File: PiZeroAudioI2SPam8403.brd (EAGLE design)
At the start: 65.1 x 30.2 mm, 46 parts, among them CON1 RPI-ZERO, J1 GROVE, J2 2X2HEADER, J3 2X1-LOCKING, J4 GROVE, J5 4X1-LOCKING, Q1 DMG2305UX, U1 TXB0104PWR, U2 LSM6DS33, U3 PCM5101A, U4 DMMT5401, U5 TXS0102, U6 PAM8403

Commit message: Fit Charger Parts
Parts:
- added C21: 4.7uF, SparkFun-Capacitors:0603
- added C25: 22uF, SparkFun-Capacitors:0805
- added D4: BLUE, SparkFun-LED:LED-0603
- added FRAME1: FRAME-LETTER, SparkFun-Aesthetics:CREATIVE_COMMONS
- added J10: (no value), SparkFun-Connectors:1X01
- added J11: AMP FCI 10103594-0001LF, SparkFun-Connectors:USB-MICROB-PTH
- added J8: JST, SparkFun-Connectors:JST-2-SMD
- added L1: 2.2UH3A, SparkFun-Coils:INDUCTOR_4X4MM
- added R10: 1k, SparkFun-Resistors:0603
- added R11, R15: 750K, SparkFun-Resistors:0603
- added R12: 100k, SparkFun-Resistors:0603
- added R13: DNP, SparkFun-Resistors:0603
- added RPROG: 2.0k, SparkFun-Resistors:0603
- added TP1: TEST-POINT3, SparkFun-Connectors:PAD.03X.03
- added U7: MCP73831, SparkFun-IC-Power:SOT23-5
- added U8: PAM2401, SparkFun-IC-Power:MSOP8
- moved U4 27.7 mm to (-70.6, 3.96)
- moved Q1 27.7 mm to (-66.7, 6.91)
- moved R7 27.7 mm to (-69.9, 6.58)
- moved R8 27.7 mm to (-66.8, 3.15)
- moved C17 25.1 mm to (-47.8, 19.8), turned to 0 degrees
- moved C16 23.9 mm to (-56.1, 19.5), turned to 180 degrees
- moved C18 23.7 mm to (-42.4, 11.4), turned to 90 degrees
- moved C20 23.7 mm to (-52.1, 19.6)
- moved C19 22.3 mm to (-59.3, 15.8), turned to 0 degrees
- moved J5 15.0 mm to (-36.7, 4.72)
- moved J3 10.6 mm to (-45.0, 4.72)
- moved U6 0.70 mm to (-48.9, 13.6)
- moved R9 0.18 mm to (-51.1, 22.9)
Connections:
- new net +5VCHARGE: C21.1, J11.VBUS, Q1.D, R10.2, U4.E2, U7.4
- new net EN: J10.1, R15.1, U8.2
- new net N$15: RPROG.1, U7.5
- new net N$16: D4.C, TP1.P$1, U7.1
- new net N$17: R11.1, R12.2, U8.5
- new net N$18: L1.P$2, U8.1
- new net N$19: R13.2, U8.6
- new net N$23: D4.A, R10.1
- new net VBATT: C25.1, J8.2, L1.P$1, R15.2, U7.3, U8.3
- net +5V: now also R11.2, U8.7; no longer Q1.D, U4.E2
- net AGND: now also C21.2, C25.2, J11.GND, J8.1, R12.1, R13.1, RPROG.2, U7.2, U8.4, U8.8
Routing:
- net +5V: track 58.3 -> 40.5 mm
- net AGND: track 66.7 -> 57.2 mm
- net GND: track 201.3 -> 196.3 mm
- net SCL-OUT: track 84.2 -> 80.5 mm
- net +5V-IN: track 7.00 -> 4.38 mm
- net SDA-OUT: track 55.0 -> 53.9 mm

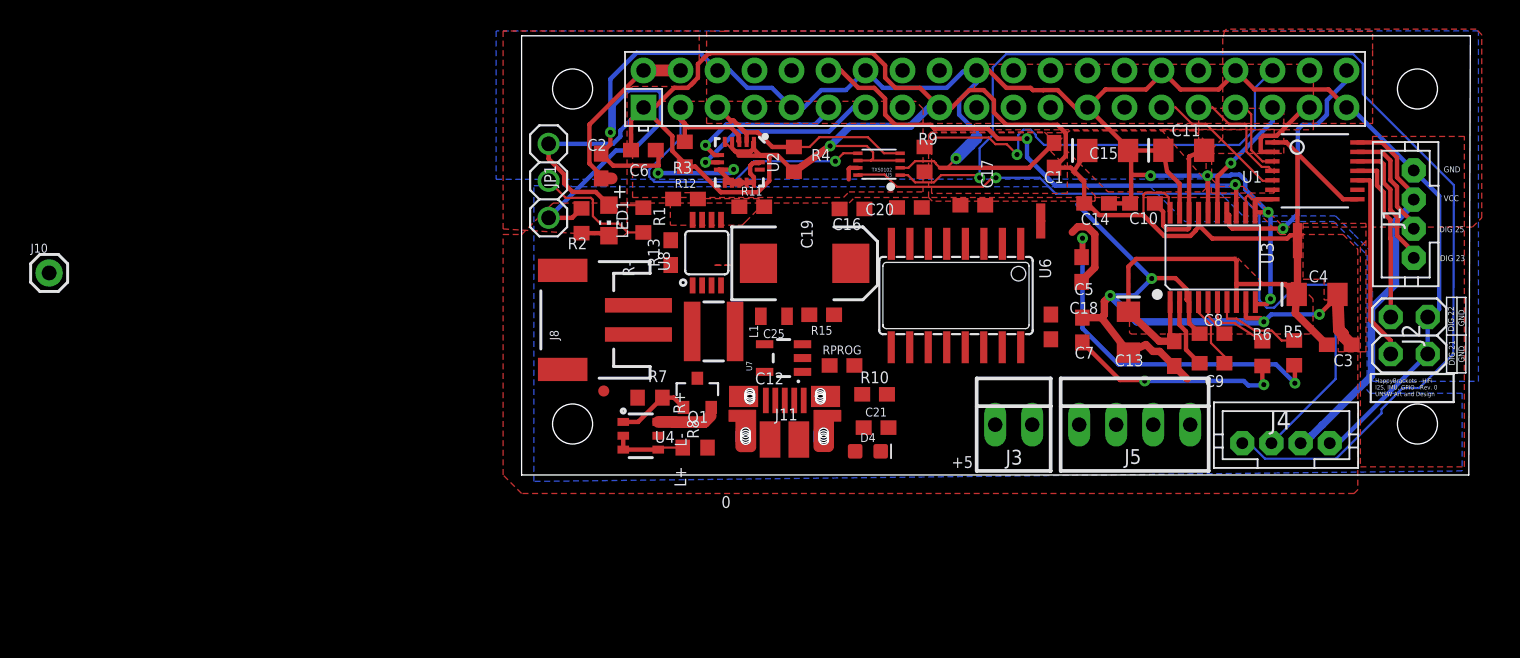
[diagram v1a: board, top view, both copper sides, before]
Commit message: Routed to Audio
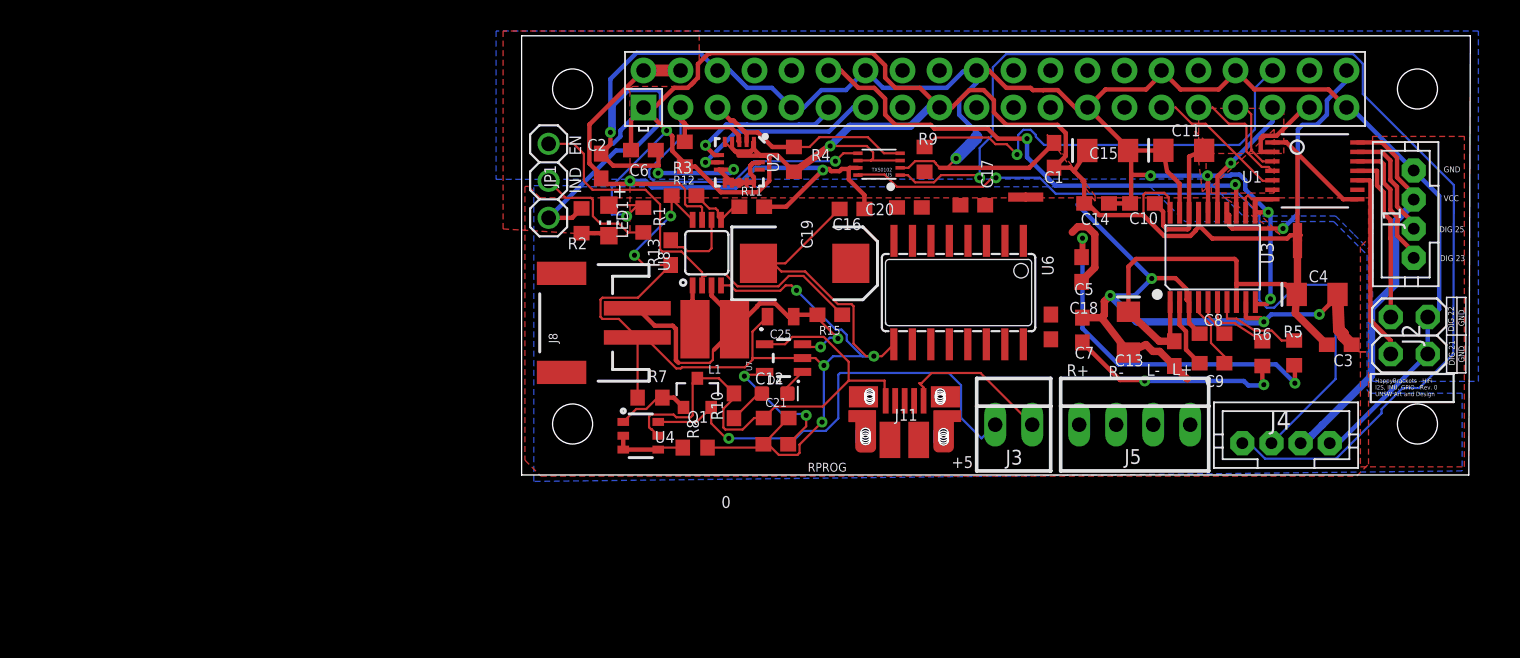
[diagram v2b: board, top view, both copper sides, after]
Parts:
- removed J10: (no value), SparkFun-Connectors:1X01
- removed TP1: TEST-POINT3, SparkFun-Connectors:PAD.03X.03
- L1: value 2.2UH3A -> IFSC1515AHER2R2M01; device SparkFun-Coils:INDUCTOR_4X4MM -> HappyBrackets:IND_IFSC_1515AH
- moved R10 9.68 mm to (-64.2, 6.02), turned to 90 degrees
- moved J11 8.23 mm to (-52.5, 5.03)
- moved D4 7.53 mm to (-61.4, 6.86)
- moved RPROG 7.07 mm to (-61.3, 3.38), turned to 180 degrees
- moved C21 6.89 mm to (-61.3, 5.18)
- moved SH2 1.85 mm to (-44.1, 20.3), turned to 0 degrees
- moved R15 0.56 mm to (-57.6, 12.3)
- moved C25 0.46 mm to (-61.0, 12.1)
- moved U6 0.27 mm to (-48.7, 13.8)
- moved R12 0.25 mm to (-67.6, 20.4)
- moved J8 0.22 mm to (-74.5, 11.7)
- moved L1 0.17 mm to (-65.5, 11.3), turned to 180 degrees
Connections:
- net N$10 renamed L-
- net N$13 renamed R-
- net N$14 renamed R+
- net N$8 renamed L+
- net +3V3: no longer JP1.1
- net AGND: now also C18.2, C19.-
- net EN: now also JP1.1; no longer J10.1
- net GND: no longer C18.2, C19.-
- net N$16: no longer TP1.P$1
- net N$18: now also L1.2; no longer L1.P$2
- net VBATT: now also L1.1; no longer L1.P$1
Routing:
- net AGND: track 57.2 -> 164.5 mm, vias 4 -> 10
- net +5VCHARGE: track 0.04 -> 35.1 mm
- net +5V: track 40.5 -> 73.7 mm, vias 0 -> 2
- net EN: track 0.00 -> 29.4 mm
- net +5V-IN: track 4.38 -> 32.2 mm, vias 0 -> 1
- net VBATT: track 0.00 -> 26.3 mm, vias 0 -> 2
- net N$15: track 0.00 -> 9.43 mm, vias 0 -> 2
- net N$19: track 0.00 -> 5.15 mm
- net N$17: track 0.00 -> 4.37 mm
- net N$18: track 0.00 -> 3.08 mm
- net N$23: track 0.00 -> 2.62 mm
- net N$16: track 0.00 -> 1.92 mm
- net +3V3: track 141.0 -> 139.3 mm, vias 1 -> 3
- removed copper zone on layer 1, net +3V3
- removed copper zone on layer 1, net +5V
- removed copper zone on layer 1, net AN3V3
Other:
- board text added: "EN"
- board text added: "IND"

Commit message: Routed with ratsnest
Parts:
- moved C18 1.78 mm to (-42.6, 9.67), turned to 270 degrees
- moved C5 1.24 mm to (-39.1, 15.7)
- moved C7 1.17 mm to (-39.1, 11.1)
- moved SH2 0.94 mm to (-44.1, 21.3), turned to 180 degrees
- moved C20 0.78 mm to (-52.9, 19.5), turned to 180 degrees
- moved C17 0.44 mm to (-47.5, 19.4)
- moved U6 0.33 mm to (-49.0, 13.6)
- moved C13 0.18 mm to (-36.9, 11.1)
- turned C16 to 0 degrees
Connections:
- net R+: now also J5.2; no longer J5.1
- net R-: now also J5.1; no longer J5.2
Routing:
- net AGND: track 164.5 -> 230.4 mm, vias 10 -> 20
- net +5V: track 73.7 -> 128.6 mm, vias 2 -> 3
- net AN3V3: track 32.2 -> 78.9 mm, vias 0 -> 3
- net AUDIO-RIGHT: track 25.1 -> 52.9 mm
- net AUDIO-LEFT: track 15.0 -> 35.6 mm, vias 2 -> 3
- net GND: track 196.3 -> 216.7 mm, vias 8 -> 10
- net L-: track 0.00 -> 20.1 mm
- net L+: track 0.00 -> 19.9 mm
- net N$5: track 0.00 -> 13.8 mm, vias 0 -> 2
- net R+: track 0.00 -> 10.4 mm
- net R-: track 0.00 -> 10.3 mm
- net +3V3: track 139.3 -> 135.3 mm
- net N$7: track 0.00 -> 2.97 mm
- added copper zone on layer 1, net +3V
- added copper zone on layer 1, net +5V

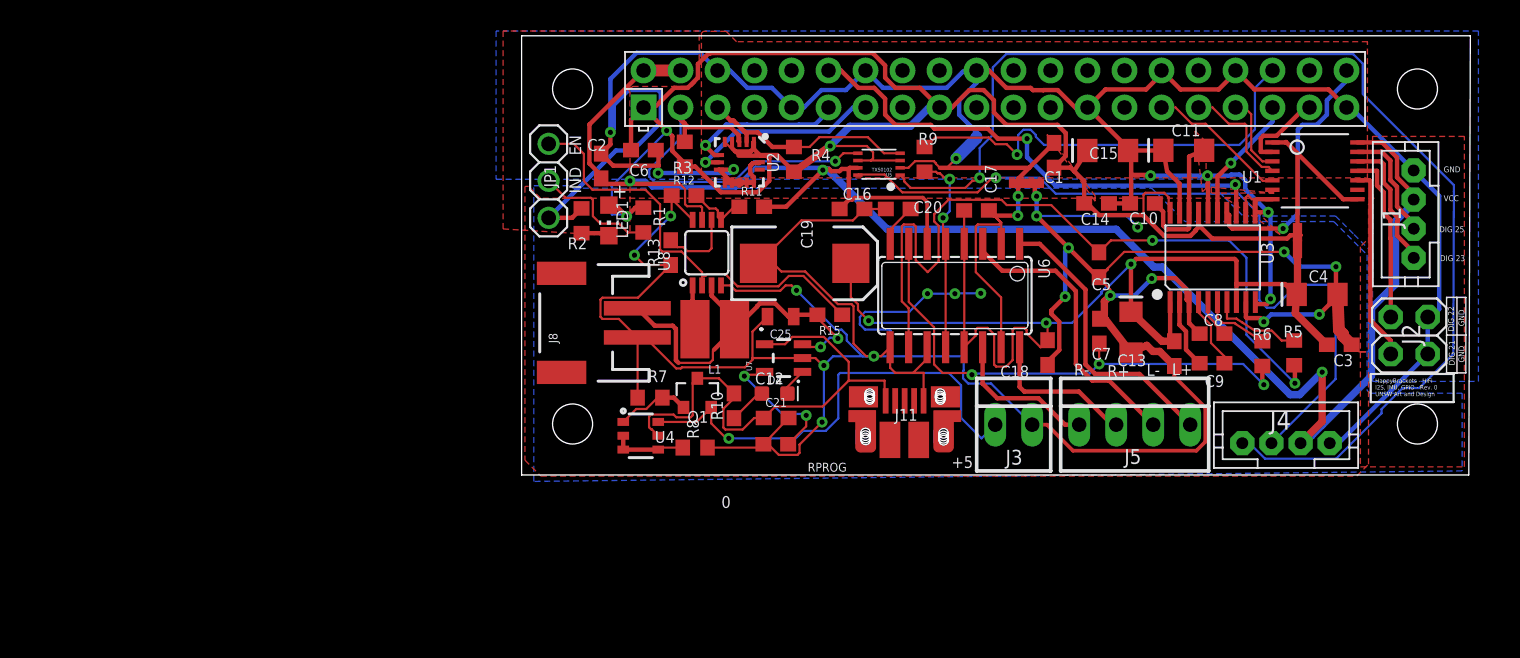
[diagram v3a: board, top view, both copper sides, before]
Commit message: Changed Footprints for consistency
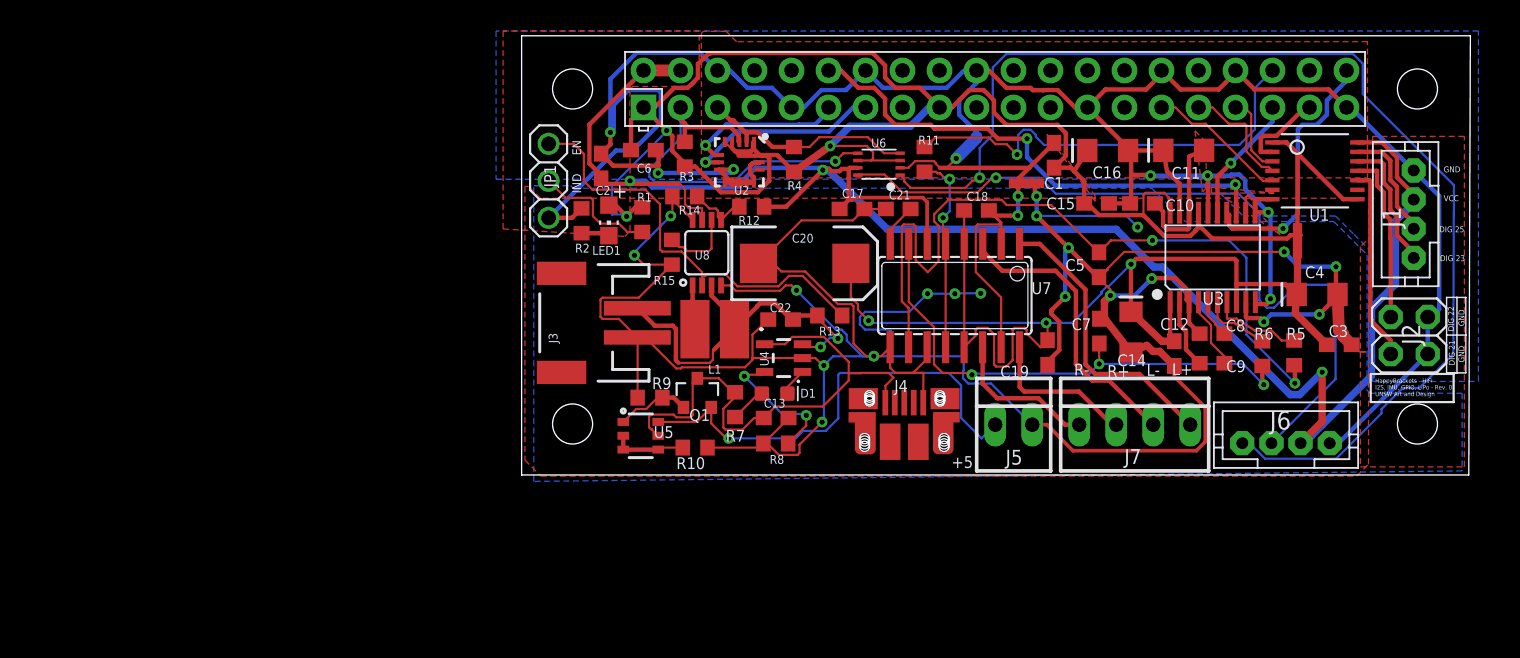
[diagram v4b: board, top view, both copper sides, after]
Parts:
- removed C25: 22uF, SparkFun-Capacitors:0805
- removed FRAME1: FRAME-LETTER, SparkFun-Aesthetics:CREATIVE_COMMONS
- removed J11: AMP FCI 10103594-0001LF, SparkFun-Connectors:USB-MICROB-PTH
- removed J8: JST, SparkFun-Connectors:JST-2-SMD
- removed RPROG: 2.0k, SparkFun-Resistors:0603
- added C22: 22uF, resistor:C0603
- added J6: GROVE, HappyBrackets:JST-PH4
- added J7: 4X1-LOCKING, HappyBrackets:22-23-2041
- added R14: 100k, adafruit:R0603
- C13: value 10uF -> 4.7uF; device HappyBrackets:EIA3216 -> SparkFun-Capacitors:0603
- C14: value 0.1uF -> 10uF; device rcl:C0603 -> HappyBrackets:EIA3216
- C15: value 10uF -> 0.1uF; device HappyBrackets:EIA3216 -> rcl:C0603
- C16: value 1uF -> 10uF; device rcl:C0603 -> HappyBrackets:EIA3216
- C19: value 470uF -> 1uF; device HappyBrackets:EIA7343 -> rcl:C0603
- C20: value 0.1uF -> 470uF; device rcl:C0603 -> HappyBrackets:EIA7343
- C21: value 4.7uF -> 0.1uF; device SparkFun-Capacitors:0603 -> rcl:C0603
- J3: value 2X1-LOCKING -> JST; device HappyBrackets:22-23-2021 -> SparkFun-Connectors:JST-2-SMD
- J4: value GROVE -> AMP FCI 10103594-0001LF; device HappyBrackets:JST-PH4 -> HappyBrackets:USB-MICROB-PTH
- J5: value 4X1-LOCKING -> 2X1-LOCKING; device HappyBrackets:22-23-2041 -> HappyBrackets:22-23-2021
- R10: value 1k -> 10K; device SparkFun-Resistors:0603 -> adafruit:R0603
- R11: value 750K -> 10K; device SparkFun-Resistors:0603 -> adafruit:R0603
- R12: value 100k -> 750K; device SparkFun-Resistors:0603 -> adafruit:R0603
- R13: value DNP -> 750K; device SparkFun-Resistors:0603 -> adafruit:R0603
- R15: value 750K -> DNP; device SparkFun-Resistors:0603 -> adafruit:R0603
- R7: value 47K -> 1k
- R8: value 10K -> 2.0k
- R9: value 10K -> 47K
- U4: value DMMT5401 -> MCP73831; device HappyBrackets:SOT26-TRANS -> SparkFun-IC-Power:SOT23-5
- U5: value TXS0102 -> DMMT5401; device adafruit:VFSOP-8 -> HappyBrackets:SOT26-TRANS
- U6: value PAM8403 -> TXS0102; device HappyBrackets:SOP-16 -> adafruit:VFSOP-8
- U7: value MCP73831 -> PAM8403; device SparkFun-IC-Power:SOT23-5 -> HappyBrackets:SOP-16
- moved J3 30.4 mm to (-74.5, 11.7), turned to 90 degrees
- moved J4 26.4 mm to (-52.5, 6.25)
- moved C13 25.1 mm to (-61.3, 5.18), turned to 0 degrees
- moved R9 25.0 mm to (-69.9, 6.58), turned to 180 degrees
- moved U5 24.8 mm to (-70.6, 3.96), turned to 270 degrees
- moved C16 18.0 mm to (-38.5, 23.5), turned to 180 degrees
- moved C19 17.8 mm to (-42.6, 9.67), turned to 270 degrees
- moved C21 16.6 mm to (-52.9, 19.5), turned to 180 degrees
- moved U7 12.5 mm to (-49.0, 13.6), turned to 180 degrees
- moved R11 12.3 mm to (-51.1, 22.9), turned to 270 degrees
- moved R13 11.7 mm to (-57.6, 12.2), turned to 180 degrees
- moved R15 11.7 mm to (-68.4, 16.6), turned to 90 degrees
- moved U4 11.2 mm to (-60.8, 9.30), turned to 90 degrees
- moved C18 10.9 mm to (-47.5, 19.4), turned to 0 degrees
- moved U6 10.4 mm to (-54.2, 22.6), turned to 90 degrees
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- renumbered D4 to D1
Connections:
- net +3V3: now also C15.2, C16.+, U6.P$3, U6.P$6; no longer C14.2, C15.+, U5.P$3, U5.P$6
- net +5V: now also C17.1, J6.3, R12.2, U6.P$7, U7.6; no longer C16.1, J4.3, R11.2, U5.P$7, U6.6
- net +5V-IN: now also J5.1, U5.E1; no longer J3.1, U4.E1
- net +5VCHARGE: now also C13.1, J4.VBUS, R7.2, U4.4, U5.E2; no longer C21.1, J11.VBUS, R10.2, U4.E2, U7.4
- net /MUTE: now also R11.1; no longer R9.1
- net AGND: now also C13.2, C14.-, C17.2, C19.2, C20.-, C22.2, J3.1, J4.GND, J5.2, R10.2, R14.1, R15.1, R9.2, U4.2, U7.11, U7.9; no longer C13.-, C16.2, C18.2, C19.-, C20.2, C25.2, J11.GND, J3.2, J8.1, R12.1, R13.1, R7.2, RPROG.2, U6.11, U6.9, U7.2
- net AN3V3: now also C14.+, C19.1, C20.+, U7.13, U7.4; no longer C13.+, C17.1, C19.+, U6.13, U6.4
- net AUDIO-LEFT: now also U7.7; no longer U6.7
- net AUDIO-RIGHT: now also U7.10; no longer U6.10
- net EN: now also R13.1; no longer R15.1
- net GND: now also C15.1, C16.-, C18.2, J6.4, U6.P$2, U7.15, U7.2; no longer C14.1, C15.-, C17.2, J4.4, U5.P$2, U6.15, U6.2
- net L+: now also J7.4, U7.1; no longer J5.4, U6.1
- net L-: now also J7.3, U7.3; no longer J5.3, U6.3
- net N$15: now also R8.1, U4.5; no longer RPROG.1, U7.5
- net N$16: now also U4.1; no longer U7.1
- net N$17: now also R12.1, R14.2; no longer R11.1, R12.2
- net N$19: now also R15.2; no longer R13.2
- net N$22: now also R10.1, U5.B1, U5.B2, U5.C2; no longer R8.1, U4.B1, U4.B2, U4.C2
- net N$23: now also R7.1; no longer R10.1
- net N$27: now also R9.1, U5.C1; no longer R7.1, U4.C1
- net N$5: now also R11.2, U7.12, U7.5; no longer R9.2, U6.12, U6.5
- net N$7: now also C21.1, U7.8; no longer C20.1, U6.8
- net R+: now also J7.2, U7.16; no longer J5.2, U6.16
- net R-: now also J7.1, U7.14; no longer J5.1, U6.14
- net SCL: now also U6.P$4; no longer U5.P$4
- net SCL-OUT: now also J6.1, U6.P$1; no longer J4.1, U5.P$1
- net SDA: now also U6.P$5; no longer U5.P$5
- net SDA-OUT: now also J6.2, U6.P$8; no longer J4.2, U5.P$8
- net VBATT: now also C22.1, J3.2, R13.2, U4.3; no longer C25.1, J8.2, R15.2, U7.3
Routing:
- net +5VCHARGE: track 35.0 -> 36.6 mm
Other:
- board text added: "HappyBrackets - HiFi I2S, IMU, GPIO, LiPo - Rev. 0 UNSW Art and Design"
- board text removed: "0"
- board text removed: "HappyBrackets - HiFi I2S, IMU, GPIO - Rev. 0 UNSW Art and Design"
